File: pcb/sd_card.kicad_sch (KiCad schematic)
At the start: 11 parts, among them J5 Micro_SD_Card_Det1, U7 AP21510FM-7, U8 TPD6F003

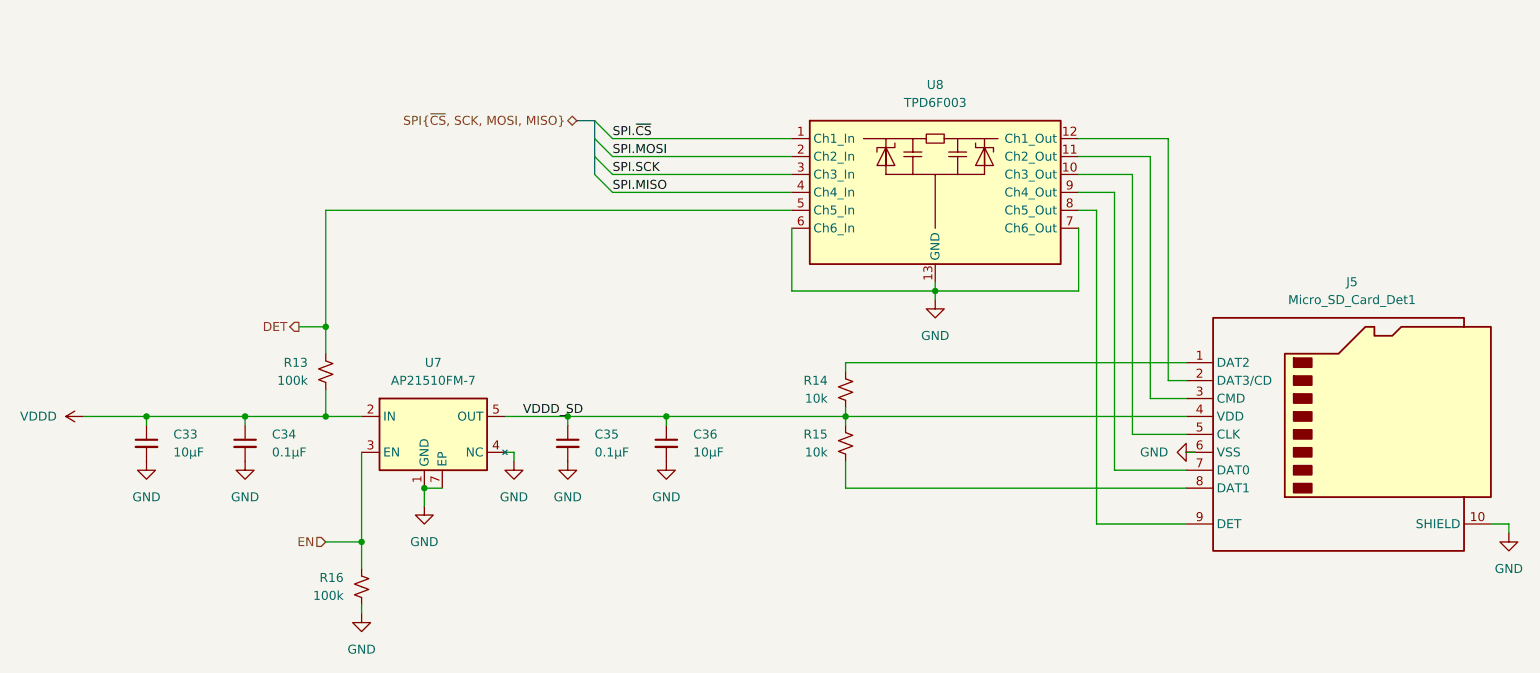
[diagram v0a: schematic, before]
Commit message: pcb: simplify power supply and define LC filter
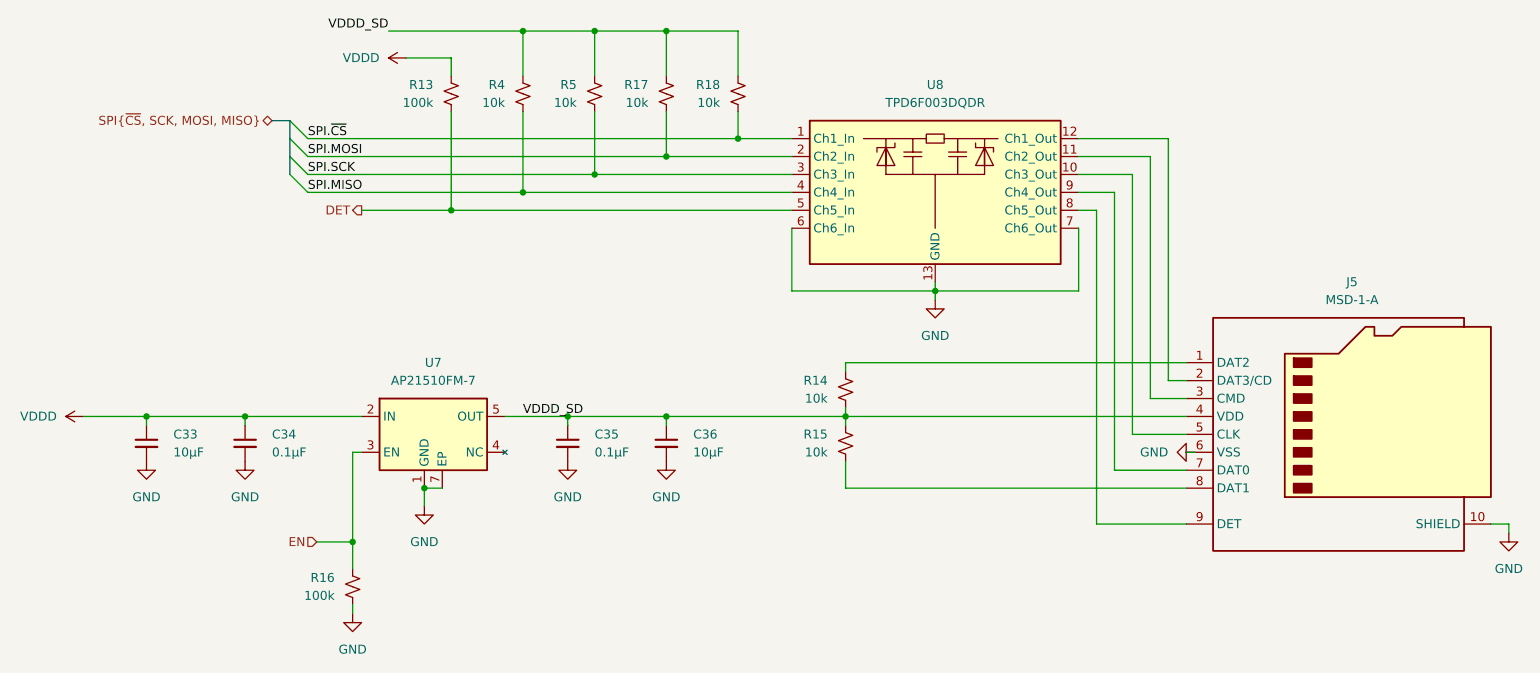
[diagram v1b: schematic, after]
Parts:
- added R17, R18, R4, R5: 10k, Resistor_SMD:R_0402_1005Metric, symbol Device:R_Small_US
- J5: value Micro_SD_Card_Det1 -> MSD-1-A
- U8: value TPD6F003 -> TPD6F003DQDR
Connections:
- net DET: now also R13.2; no longer R13.1
- net GND: no longer U7.4 (NC)
- net SPI.MISO: now also R4.2
- net SPI.MOSI: now also R17.2
- net SPI.SCK: now also R5.2
- net SPI.~{CS}: now also R18.2
- net VDDD: now also R13.1; no longer R13.2
- net VDDD_SD: now also R17.1, R18.1, R4.1, R5.1
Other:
- moved on the sheet: R16

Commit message: pcb: pretty much the final version
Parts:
- C33, C36: manf# (none) -> GRM188R61A106ME69D
- C34, C35: manf# (none) -> CL05A104KA5NNNC
- J5: manf# (none) -> MSD-1-A
- R13, R16: manf# (none) -> WR04X1003FTL
- R14, R15, R17, R18, R4, R5: manf# (none) -> CR0402-JW-103GLF
- U7: manf# (none) -> AP21510FM-7
- U8: digikey# (none) -> 296-25802-1-ND; manf# (none) -> TPD6F003DQDR
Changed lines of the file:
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@@
 			)
 		)
-		(property "Description" "Pull-up"
+		(property "Description" "Resistor, pull-up"
+			(at 128.27 38.1 0)
+			(effects
+				(font
+					(size 1.27 1.27)
+				)
+				(hide yes)
+			)
+		)
+		(property "manf#" "CR0402-JW-103GLF"
 			(at 128.27 38.1 0)
 			(effects
@@
 			)
 		)
+		(property "manf#" "AP21510FM-7 "
+			(at 85.09 86.36 0)
+			(effects
+				(font
+					(size 1.27 1.27)
+				)
+				(hide yes)
+			)
+		)
 		(pin "5"
 		)
@@
 			)
 		)
-		(property "Description" "Pull-up"
+		(property "Description" "Resistor, pull-up"
+			(at 107.95 38.1 0)
+			(effects
+				(font
+					(size 1.27 1.27)
+				)
+				(hide yes)
+			)
+		)
+		(property "manf#" "CR0402-JW-103GLF"
 			(at 107.95 38.1 0)
 			(effects
@@
 			)
 		)
-		(property "Description" "Pull-up"
+		(property "Description" "Resistor, pull-up"
+			(at 97.79 38.1 0)
+			(effects
+				(font
+					(size 1.27 1.27)
+				)
+				(hide yes)
+			)
+		)
+		(property "manf#" "CR0402-JW-103GLF"
 			(at 97.79 38.1 0)
 			(effects
@@
 			)
 		)
-		(property "Description" "Pull-up"
+		(property "Description" "Resistor, pull-down"
+			(at 73.66 107.95 0)
+			(effects
+				(font
+					(size 1.27 1.27)
+				)
+				(hide yes)
+			)
+		)
+		(property "manf#" "WR04X1003FTL"
 			(at 73.66 107.95 0)
 			(effects
@@
 			)
 		)
+		(property "manf#" "MSD-1-A"
+			(at 214.63 86.36 0)
+			(effects
+				(font
+					(size 1.27 1.27)
+				)
+				(hide yes)
+			)
+		)
 		(pin "7"
 		)
@@
 			)
 		)
-		(property "Description" "Pull-up"
+		(property "Description" "Resistor, pull-up"
+			(at 87.63 38.1 0)
+			(effects
+				(font
+					(size 1.27 1.27)
+				)
+				(hide yes)
+			)
+		)
+		(property "manf#" "WR04X1003FTL"
 			(at 87.63 38.1 0)
 			(effects
@@
 			)
 		)
-		(property "Description" "Capacitor, 16V, X7R"
+		(property "Description" "Capacitor, decoupling, 10V, X5R"
+			(at 44.45 87.63 0)
+			(effects
+				(font
+					(size 1.27 1.27)
+				)
+				(hide yes)
+			)
+		)
+		(property "manf#" "GRM188R61A106ME69D"
 			(at 44.45 87.63 0)
 			(effects
@@
 			)
 		)
-		(property "Description" "Capacitor, 16V, X7R"
+		(property "Description" "Capacitor, decoupling, 10V, X5R"
+			(at 118.11 87.63 0)
+			(effects
+				(font
+					(size 1.27 1.27)
+				)
+				(hide yes)
+			)
+		)
+		(property "manf#" "GRM188R61A106ME69D"
 			(at 118.11 87.63 0)
 			(effects
@@
 			)
 		)
+		(property "manf#" "TPD6F003DQDR"
+			(at 156.21 52.07 0)
+			(effects
+				(font
+					(size 1.27 1.27)
+				)
+				(hide yes)
+			)
+		)
+		(property "digikey#" "296-25802-1-ND"
+			(at 156.21 52.07 0)
+			(effects
+				(font
+					(size 1.27 1.27)
+				)
+				(hide yes)
+			)
+		)
 		(pin "2"
 		)
@@
 			)
 		)
-		(property "Description" "Pull-up"
+		(property "Description" "Resistor, pull-up"
+			(at 143.51 80.01 0)
+			(effects
+				(font
+					(size 1.27 1.27)
+				)
+				(hide yes)
+			)
+		)
+		(property "manf#" "CR0402-JW-103GLF"
 			(at 143.51 80.01 0)
 			(effects
@@
 			)
 		)
-		(property "Description" "Pull-up"
+		(property "Description" "Resistor, pull-up"
+			(at 143.51 87.63 0)
+			(effects
+				(font
+					(size 1.27 1.27)
+				)
+				(hide yes)
+			)
+		)
+		(property "manf#" "CR0402-JW-103GLF"
 			(at 143.51 87.63 0)
 			(effects
@@
 			)
 		)
-		(property "Description" "Pull-up"
+		(property "Description" "Resistor, pull-up"
+			(at 118.11 38.1 0)
+			(effects
+				(font
+					(size 1.27 1.27)
+				)
+				(hide yes)
+			)
+		)
+		(property "manf#" "CR0402-JW-103GLF"
 			(at 118.11 38.1 0)
 			(effects
@@
 			)
 		)
-		(property "Description" "Capacitor, decoupling"
+		(property "Description" "Capacitor, decoupling, 25V, X5R"
+			(at 104.14 87.63 0)
+			(effects
+				(font
+					(size 1.27 1.27)
+				)
+				(hide yes)
+			)
+		)
+		(property "manf#" "CL05A104KA5NNNC"
 			(at 104.14 87.63 0)
 			(effects
@@
 			)
 		)
-		(property "Description" "Capacitor, decoupling"
+		(property "Description" "Capacitor, decoupling, 25V, X5R"
 			(at 58.42 87.63 0)
 			(effects
+				(font
+					(size 1.27 1.27)
+				)
+				(hide yes)
+			)
+		)
+		(property "manf#" "CL05A104KA5NNNC"
+			(at 58.42 87.63 0)
+			(effects
